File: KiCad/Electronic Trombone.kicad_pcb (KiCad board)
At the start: 2 copper layers, 148 parts, among them J1 691137710004, J2 691137710003, J3 691137710003, J4 691137710002, Q1 NPN, Q2 PNP, Q3 NPN, Q4 PNP, Q5 NPN, Q6 NPN, SW1 SW_Push, SW2 SW_Push, SW3 SW_Push, U1 CD74HC4051E, U10 TL074, U2 TL074, U3 TL074, U4 40106, U5 TL074, U6 TL074, U7 TL074, U8 TL074, U9 TL074

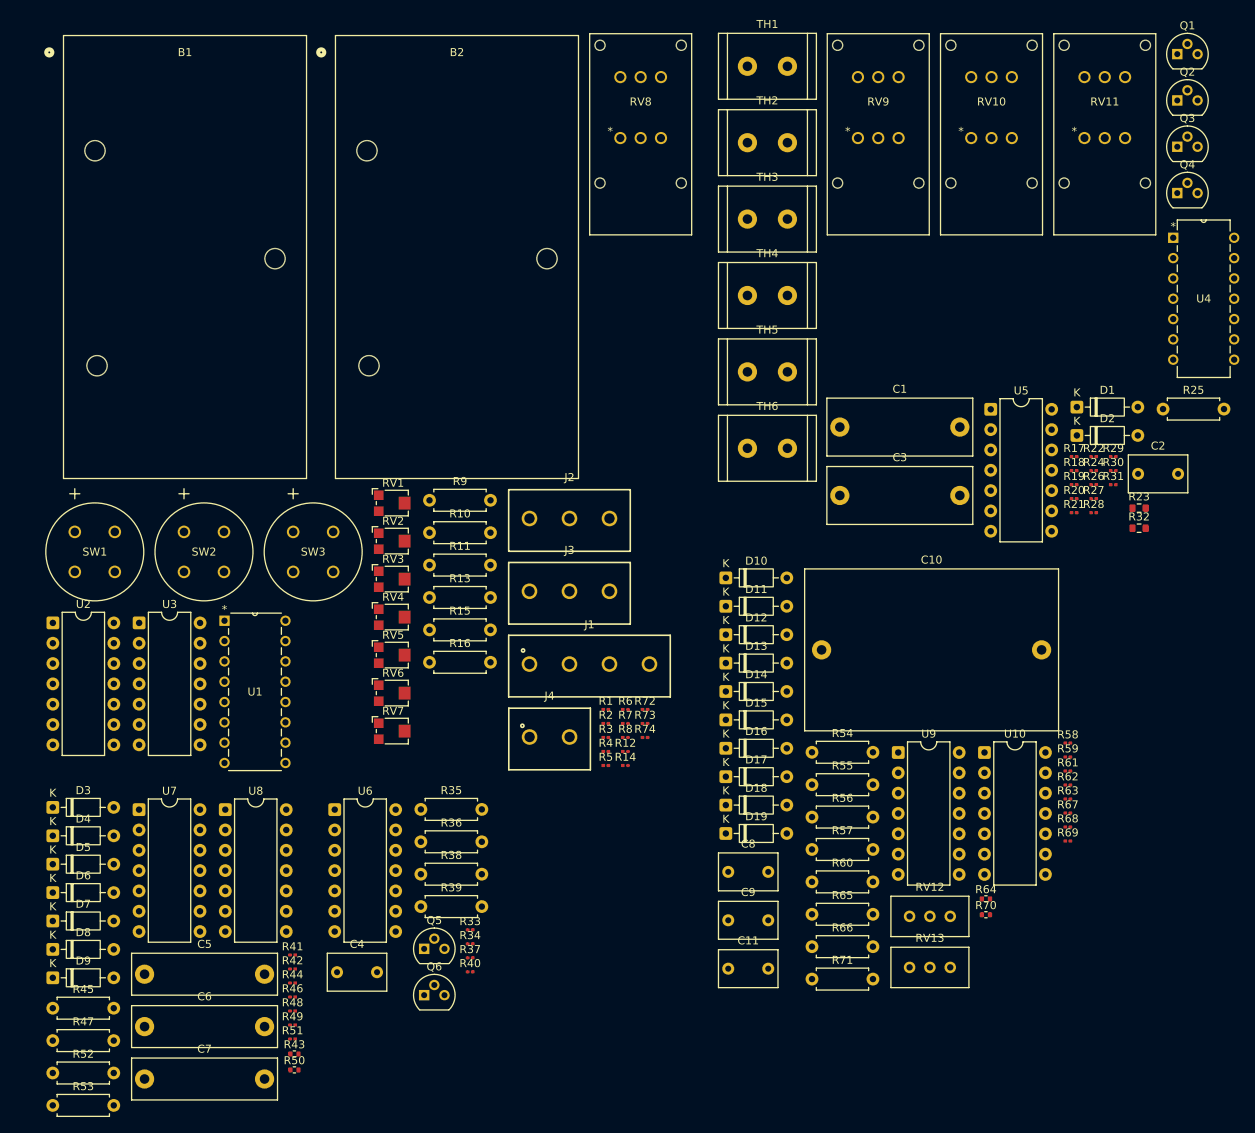
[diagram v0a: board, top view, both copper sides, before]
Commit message: added power switch, decoupling caps, and unused IC pins
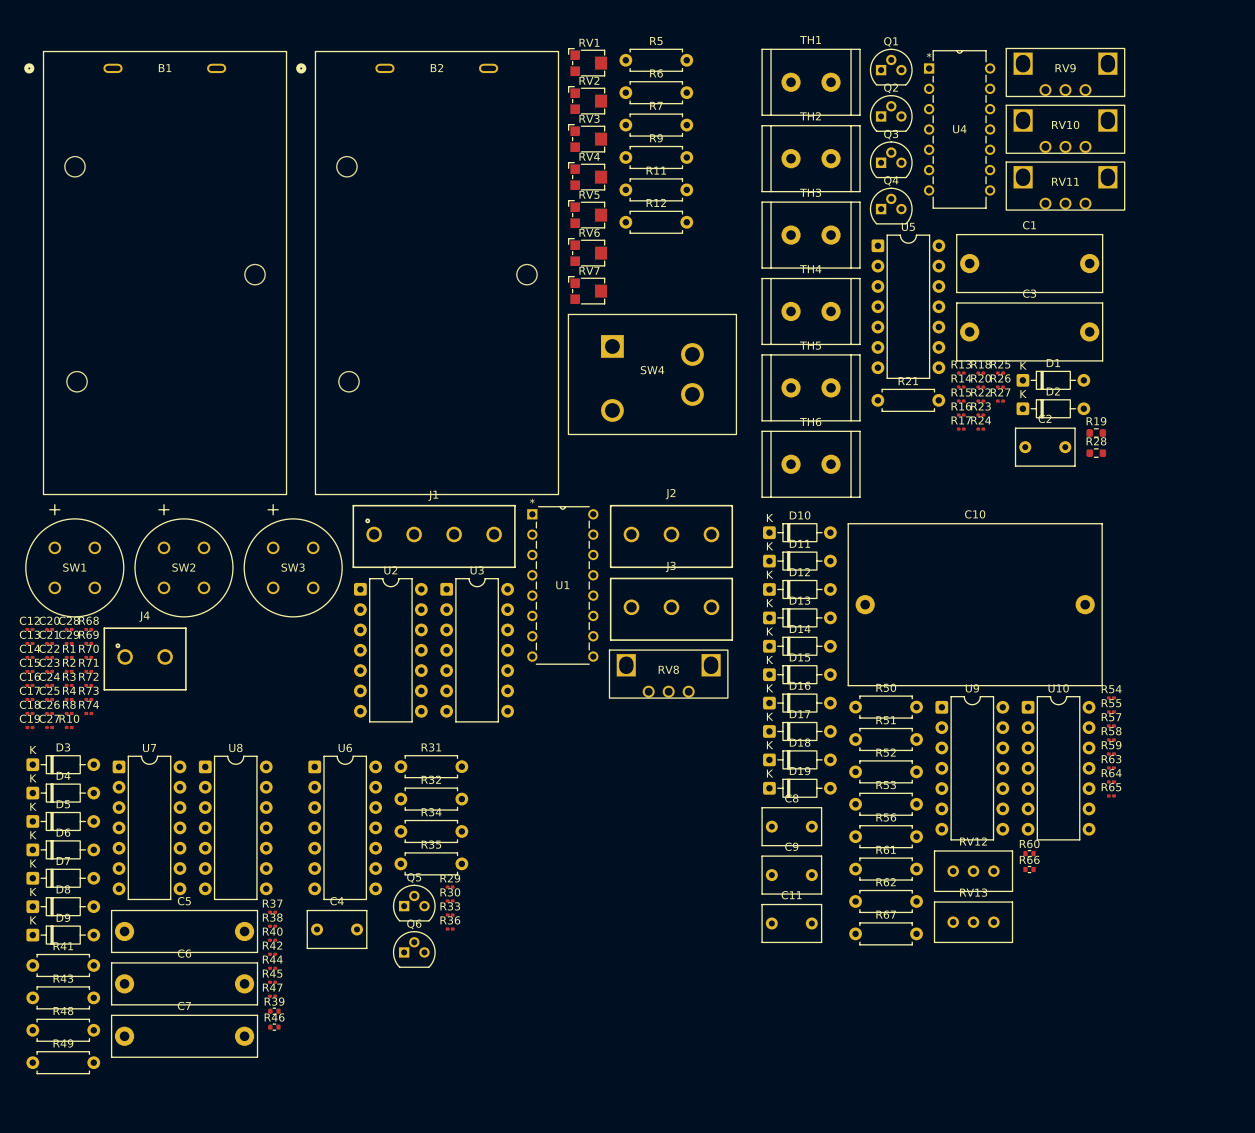
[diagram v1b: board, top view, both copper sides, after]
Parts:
- added C12: 0.1u, Capacitor_SMD:C_0201_0603Metric, F.Cu at (21.2, 98.7)
- added C13: 0.1u, Capacitor_SMD:C_0201_0603Metric, F.Cu at (21.2, 100.4)
- added C14: 0.1u, Capacitor_SMD:C_0201_0603Metric, F.Cu at (21.2, 102.2)
- added C15: 0.1u, Capacitor_SMD:C_0201_0603Metric, F.Cu at (21.2, 103.9)
- added C16: 0.1u, Capacitor_SMD:C_0201_0603Metric, F.Cu at (21.2, 105.7)
- added C17: 0.1u, Capacitor_SMD:C_0201_0603Metric, F.Cu at (21.2, 107.4)
- added C18: 0.1u, Capacitor_SMD:C_0201_0603Metric, F.Cu at (21.2, 109.2)
- added C19: 0.1u, Capacitor_SMD:C_0201_0603Metric, F.Cu at (21.2, 110.9)
- added C20: 0.1u, Capacitor_SMD:C_0201_0603Metric, F.Cu at (23.7, 98.7)
- added C21: 0.1u, Capacitor_SMD:C_0201_0603Metric, F.Cu at (23.7, 100.4)
- added C22: 0.1u, Capacitor_SMD:C_0201_0603Metric, F.Cu at (23.7, 102.2)
- added C23: 0.1u, Capacitor_SMD:C_0201_0603Metric, F.Cu at (23.7, 103.9)
- added C24: 0.1u, Capacitor_SMD:C_0201_0603Metric, F.Cu at (23.7, 105.7)
- added C25: 0.1u, Capacitor_SMD:C_0201_0603Metric, F.Cu at (23.7, 107.4)
- added C26: 0.1u, Capacitor_SMD:C_0201_0603Metric, F.Cu at (23.7, 109.2)
- added C27: 0.1u, Capacitor_SMD:C_0201_0603Metric, F.Cu at (23.7, 110.9)
- added C28: 0.1u, Capacitor_SMD:C_0201_0603Metric, F.Cu at (26.1, 98.7)
- added C29: 0.1u, Capacitor_SMD:C_0201_0603Metric, F.Cu at (26.1, 100.4)
- added SW4: SW_DPST, DPST Switch RA83231100:DPST Switch RA83231100, F.Cu at (99.0, 66.8)
- R1, R4: value 12k -> 10k
- R10, R36: value R_US -> 10k; footprint Resistor_THT:R_Axial_DIN0207_L6.3mm_D2.5mm_P7.62mm_Horizontal -> Resistor_SMD:R_0201_0603Metric
- R12, R5, R6, R7: value 10k -> R_US; footprint Resistor_SMD:R_0201_0603Metric -> Resistor_THT:R_Axial_DIN0207_L6.3mm_D2.5mm_P7.62mm_Horizontal
- R13, R15, R38, R45, R47, R65: value R_US -> 30k; footprint Resistor_THT:R_Axial_DIN0207_L6.3mm_D2.5mm_P7.62mm_Horizontal -> Resistor_SMD:R_0201_0603Metric
- R14: value 10k -> 100k
- R16, R25: value R_US -> 1M; footprint Resistor_THT:R_Axial_DIN0207_L6.3mm_D2.5mm_P7.62mm_Horizontal -> Resistor_SMD:R_0201_0603Metric
- R17, R26: value 30k -> 1M
- R19, R28: value 30k -> 2.5k; footprint Resistor_SMD:R_0201_0603Metric -> Resistor_SMD:R_0603_1608Metric
- R2, R3: value 15k -> 10k
- R20, R29, R30: value 1M -> 100k
- R21: value 1M -> R_US; footprint Resistor_SMD:R_0201_0603Metric -> Resistor_THT:R_Axial_DIN0207_L6.3mm_D2.5mm_P7.62mm_Horizontal
- R22, R24, R37, R58, R59: value 100k -> 30k
- R23: value 2.5k -> 100k; footprint Resistor_SMD:R_0603_1608Metric -> Resistor_SMD:R_0201_0603Metric
- R31, R34: value 100k -> R_US; footprint Resistor_SMD:R_0201_0603Metric -> Resistor_THT:R_Axial_DIN0207_L6.3mm_D2.5mm_P7.62mm_Horizontal
- R32: value 2.5k -> R_US; footprint Resistor_SMD:R_0603_1608Metric -> Resistor_THT:R_Axial_DIN0207_L6.3mm_D2.5mm_P7.62mm_Horizontal
- R39, R60, R66: value R_US -> 1k; footprint Resistor_THT:R_Axial_DIN0207_L6.3mm_D2.5mm_P7.62mm_Horizontal -> Resistor_SMD:R_0402_1005Metric
- R40: value 10k -> 30k
- R41, R48, R49, R51, R62: value 30k -> R_US; footprint Resistor_SMD:R_0201_0603Metric -> Resistor_THT:R_Axial_DIN0207_L6.3mm_D2.5mm_P7.62mm_Horizontal
- R43, R50: value 1k -> R_US; footprint Resistor_SMD:R_0402_1005Metric -> Resistor_THT:R_Axial_DIN0207_L6.3mm_D2.5mm_P7.62mm_Horizontal
- R46: value 30k -> 1k; footprint Resistor_SMD:R_0201_0603Metric -> Resistor_SMD:R_0402_1005Metric
- R54, R55: value R_US -> 100k; footprint Resistor_THT:R_Axial_DIN0207_L6.3mm_D2.5mm_P7.62mm_Horizontal -> Resistor_SMD:R_0201_0603Metric
- R57: value R_US -> 510; footprint Resistor_THT:R_Axial_DIN0207_L6.3mm_D2.5mm_P7.62mm_Horizontal -> Resistor_SMD:R_0201_0603Metric
- R61, R67: value 510 -> R_US; footprint Resistor_SMD:R_0201_0603Metric -> Resistor_THT:R_Axial_DIN0207_L6.3mm_D2.5mm_P7.62mm_Horizontal
- R63: value 30k -> 510
- R64, R70: value 1k -> 30k; footprint Resistor_SMD:R_0402_1005Metric -> Resistor_SMD:R_0201_0603Metric
- R71: value R_US -> 15k; footprint Resistor_THT:R_Axial_DIN0207_L6.3mm_D2.5mm_P7.62mm_Horizontal -> Resistor_SMD:R_0201_0603Metric
- R72, R73: value 30k -> 12k
- R74: value 30k -> 15k
- RV10, RV11, RV8, RV9: footprint Potentiometer 51CAD_E24_A20L:POT_51CAD_12P5X13P25_BRN -> Potentiometer 100k PTV09A-2020F-B104:Potentiometer 100k PTV09A-2020F-B104
- SW1, SW2, SW3: value SW_Push -> SW_Push_Dual
- moved R68 124.8 mm to (28.6, 98.7)
- moved R69 124.8 mm to (28.6, 100.4)
- moved R70 116.7 mm to (28.6, 102.2)
- moved R52 107.2 mm to (124.4, 116.5)
- moved R53 107.2 mm to (124.4, 120.5)
- moved R29 98.8 mm to (73.7, 130.9)
- moved R30 98.8 mm to (73.7, 132.6)
- moved R32 98.3 mm to (67.6, 119.9)
- moved R71 98.2 mm to (28.6, 103.9)
- moved R31 95.8 mm to (67.6, 115.8)
- moved R5 88.2 mm to (95.7, 27.5)
- moved R50 83.5 mm to (124.4, 108.4)
- moved R51 79.7 mm to (124.4, 112.4)
- moved R6 77.1 mm to (95.7, 31.6)
- moved R7 74.8 mm to (95.7, 35.6)
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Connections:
- net Net-(D1-A) renamed //Oscillator/Sch Inv Out 1
- D2 pad 2: Net-(D2-A) -> //Oscillator/Sch Inv Out 2
- R1 pad 1: +5V -> //-Pot
- R1 pad 2: +9V -> Net-(U2B-+)
- R10 pad 1: GND -> Net-(R10-Pad1)
- R10 pad 2: Net-(U2C--) -> Net-(U3C-+)
- R11 pad 2: Net-(R11-Pad2) -> //Amp Control
- R12 pad 1: Net-(U3D-+) -> //Envelope Generator/Out Amp
- R12 pad 2: //Filter Control -> Net-(U3B-+)
- R13 pad 1: //Envelope Generator/Out Filter -> Net-(R13-Pad1)
- R13 pad 2: Net-(U3B-+) -> GND
- R14 pad 1: Net-(R11-Pad2) -> Net-(R13-Pad1)
- R14 pad 2: Net-(U3D-+) -> Net-(R14-Pad2)
- R15 pad 1: Net-(U3C-+) -> -9V
- R15 pad 2: //Amp Control -> Net-(R13-Pad1)
- R16 pad 1: //Envelope Generator/Out Amp -> +9V
- R16 pad 2: Net-(U3C-+) -> Net-(Q1-B)
- R17 pad 2: GND -> Net-(R17-Pad2)
- R18 pad 1: Net-(R17-Pad1) -> //Oscillator/In
- R19 pad 1: -9V -> //Oscillator/Core In 1
- R19 pad 2: Net-(R17-Pad1) -> GND
- R2 pad 1: -5V -> Net-(U2B-+)
- R2 pad 2: GND -> //+Pot
- R20 pad 1: +9V -> Net-(C2-Pad2)
- R20 pad 2: Net-(Q1-B) -> Net-(U5C-+)
- R21 pad 1: Net-(R21-Pad1) -> GND
- R21 pad 2: Net-(R21-Pad2) -> Net-(U5C-+)
- R22 pad 1: //Oscillator/In -> Net-(R22-Pad1)
- R22 pad 2: Net-(R22-Pad2) -> GND
- R23 pad 1: //Oscillator/Core In 1 -> Net-(R22-Pad1)
- R23 pad 2: GND -> Net-(R23-Pad2)
- R24 pad 1: Net-(C2-Pad2) -> -9V
- R24 pad 2: Net-(U5C-+) -> Net-(R22-Pad1)
- R25 pad 1: GND -> +9V
- R25 pad 2: Net-(U5C-+) -> Net-(Q3-B)
- R26 pad 2: GND -> Net-(R26-Pad2)
- R27 pad 1: Net-(R26-Pad1) -> //Oscillator/In
- R28 pad 1: -9V -> //Oscillator/Core In 2
- R28 pad 2: Net-(R26-Pad1) -> GND
- R29 pad 2: Net-(Q3-B) -> Net-(Q5-C)
- R3 pad 2: +5V -> Net-(U2B--)
- R30 pad 1: Net-(R30-Pad1) -> +9V
- R30 pad 2: Net-(R30-Pad2) -> Net-(Q6-C)
- R31 pad 1: //Oscillator/In -> Net-(U6C--)
- R31 pad 2: Net-(R31-Pad2) -> Net-(C4-Pad1)
- R32 pad 1: //Oscillator/Core In 2 -> Net-(U6A--)
- R32 pad 2: GND -> Net-(U6C--)
- R33 pad 1: +9V -> Net-(U6D-+)
- R33 pad 2: Net-(Q5-C) -> GND
- R34 pad 1: +9V -> Net-(U6B--)
- R34 pad 2: Net-(Q6-C) -> Net-(U6C-+)
- R35 pad 1: Net-(U6C--) -> Net-(U6C-+)
- R35 pad 2: Net-(C4-Pad1) -> GND
- R36 pad 1: Net-(U6A--) -> Net-(Q5-E)
- R36 pad 2: Net-(U6C--) -> //Amp Control
- R37 pad 1: Net-(U6D-+) -> Net-(U7B--)
- R37 pad 2: GND -> Net-(D3-A)
- R38 pad 1: Net-(U6B--) -> //Filter/Signal In
- R38 pad 2: Net-(U6C-+) -> Net-(U7B--)
- R39 pad 1: Net-(U6C-+) -> Net-(D3-A)
- R39 pad 2: GND -> Net-(R39-Pad2)
- R4 pad 1: -9V -> Net-(U2B--)
- R4 pad 2: -5V -> //Pot Voltage Difference
- R40 pad 1: Net-(Q5-E) -> Net-(U7B-+)
- R40 pad 2: //Amp Control -> //Filter/Processed Control
- R41 pad 1: Net-(U7B--) -> Net-(D5-A)
- R41 pad 2: Net-(D3-A) -> //Filter Control
- R42 pad 1: //Filter/Signal In -> GND
- R42 pad 2: Net-(U7B--) -> Net-(U7B-+)
- R43 pad 1: Net-(D3-A) -> GND
- R43 pad 2: Net-(R43-Pad2) -> Net-(D5-A)
- R44 pad 1: Net-(U7B-+) -> Net-(U7C--)
- R44 pad 2: //Filter/Processed Control -> Net-(D9-K)
- R45 pad 1: Net-(D5-A) -> //Filter/Signal In
- R45 pad 2: //Filter Control -> Net-(U7C--)
- R46 pad 1: GND -> Net-(D9-K)
- R46 pad 2: Net-(U7B-+) -> Net-(R46-Pad2)
- R47 pad 1: GND -> //Filter/Processed Control
- R47 pad 2: Net-(D5-A) -> Net-(U7C--)
- R48 pad 1: Net-(U7C--) -> Net-(U8B--)
- R48 pad 2: Net-(D9-K) -> Net-(U8C-+)
- R49 pad 1: //Filter/Signal In -> Net-(U8A--)
- R49 pad 2: Net-(U7C--) -> Net-(U8B--)
- R5 pad 1: //-Pot -> Net-(U2C--)
- R5 pad 2: Net-(U2B-+) -> Net-(R5-Pad2)
- R50 pad 1: Net-(D9-K) -> Net-(D10-K)
- R50 pad 2: Net-(R50-Pad2) -> //Envelope Generator/Sustain Voltage Amp
- R51 pad 1: //Filter/Processed Control -> //Envelope Generator/Sustain Voltage Amp
- R51 pad 2: Net-(U7C--) -> GND
- R52 pad 1: Net-(U8B--) -> Net-(D11-K)
- R52 pad 2: Net-(U8C-+) -> //Envelope Generator/Sustain Voltage Filter
- R53 pad 1: Net-(U8A--) -> //Envelope Generator/Sustain Voltage Filter
- R53 pad 2: Net-(U8B--) -> GND
- R54 pad 1: Net-(D10-K) -> GND
- R54 pad 2: //Envelope Generator/Sustain Voltage Amp -> //Envelope Generator/Trigger Ref
- R55 pad 1: //Envelope Generator/Sustain Voltage Amp -> //Envelope Generator/Trigger Ref
- R55 pad 2: GND -> -9V
- R56 pad 1: Net-(D11-K) -> Net-(D12-K)
- R56 pad 2: //Envelope Generator/Sustain Voltage Filter -> Net-(U10B-+)
- R57 pad 1: //Envelope Generator/Sustain Voltage Filter -> Net-(D13-A)
- R57 pad 2: GND -> Net-(R57-Pad2)
- R58 pad 1: GND -> Net-(D13-K)
- R58 pad 2: //Envelope Generator/Trigger Ref -> GND
- R59 pad 1: //Envelope Generator/Trigger Ref -> Net-(D14-K)
- R59 pad 2: -9V -> //Envelope Generator/Sustain Voltage Filter
- R6 pad 1: Net-(U2B-+) -> GND
- R6 pad 2: //+Pot -> Net-(U2C--)
- R60 pad 1: Net-(D12-K) -> Net-(R60-Pad1)
- R60 pad 2: Net-(U10B-+) -> //Envelope Generator/Out Amp
- R61 pad 1: Net-(D13-A) -> Net-(D15-A)
- R61 pad 2: Net-(R61-Pad2) -> Net-(U10B-+)
- R62 pad 1: Net-(D13-K) -> Net-(D16-K)
- R62 pad 2: GND -> Net-(U10D-+)
- R63 pad 1: Net-(D14-K) -> Net-(D17-A)
- R63 pad 2: //Envelope Generator/Sustain Voltage Filter -> Net-(R63-Pad2)
- R64 pad 1: Net-(R64-Pad1) -> Net-(D17-K)
- R64 pad 2: //Envelope Generator/Out Amp -> GND
- R65 pad 1: Net-(D15-A) -> Net-(D18-K)
- R65 pad 2: Net-(U10B-+) -> //Envelope Generator/Sustain Voltage Amp
- R66 pad 1: Net-(D16-K) -> Net-(R66-Pad1)
- R66 pad 2: Net-(U10D-+) -> //Envelope Generator/Out Filter
- R67 pad 1: Net-(D17-A) -> Net-(D19-A)
- R67 pad 2: Net-(R67-Pad2) -> Net-(U10D-+)
- R68 pad 1: Net-(D17-K) -> Net-(J3-Pad1)
- R69 pad 1: Net-(D18-K) -> Net-(J3-Pad2)
- R69 pad 2: //Envelope Generator/Sustain Voltage Amp -> GND
- R7 pad 1: GND -> Net-(U3A-+)
- R7 pad 2: Net-(U2B--) -> Net-(R10-Pad1)
- R70 pad 1: Net-(R70-Pad1) -> Net-(J3-Pad3)
- R70 pad 2: //Envelope Generator/Out Filter -> GND
- R71 pad 1: Net-(D19-A) -> -5V
- R71 pad 2: Net-(U10D-+) -> GND
- R72 pad 1: Net-(J3-Pad1) -> +5V
- R72 pad 2: GND -> +9V
- R73 pad 1: Net-(J3-Pad2) -> -9V
- R73 pad 2: GND -> -5V
- R74 pad 1: Net-(J3-Pad3) -> GND
- R74 pad 2: GND -> +5V
- R8 pad 1: Net-(U2B--) -> Net-(U3C-+)
- R8 pad 2: //Pot Voltage Difference -> //Filter Control
- R9 pad 1: Net-(U2C--) -> //Envelope Generator/Out Filter
- R9 pad 2: Net-(R9-Pad2) -> Net-(U3A-+)
- RV11 pad 2: Net-(R30-Pad1) -> Net-(R26-Pad1)
- RV12 pad 1: Net-(R61-Pad2) -> Net-(R57-Pad2)
- RV12 pad 2: Net-(R61-Pad2) -> Net-(R57-Pad2)
- RV13 pad 1: Net-(R67-Pad2) -> Net-(R63-Pad2)
- RV13 pad 2: Net-(R67-Pad2) -> Net-(R63-Pad2)
- RV8 pad 1: Net-(R9-Pad2) -> Net-(R5-Pad2)
- RV9 pad 2: Net-(R21-Pad1) -> Net-(R17-Pad1)
- SW1 pad 3: (no net) -> +5V
- SW1 pad 4: (no net) -> Net-(J3-Pad1)
- SW2 pad 3: (no net) -> +5V
- SW2 pad 4: (no net) -> Net-(J3-Pad2)
- SW3 pad 3: (no net) -> +5V
- SW3 pad 4: (no net) -> Net-(J3-Pad3)
- TH1 pad 1: Net-(R18-Pad2) -> Net-(R14-Pad2)
- TH2 pad 1: Net-(R21-Pad2) -> Net-(R17-Pad2)
- TH3 pad 1: Net-(R22-Pad2) -> Net-(R18-Pad2)
- TH4 pad 1: Net-(R27-Pad2) -> Net-(R23-Pad2)
- TH5 pad 1: Net-(R30-Pad2) -> Net-(R26-Pad2)
- TH6 pad 1: Net-(R31-Pad2) -> Net-(R27-Pad2)
- U10 pad 11: (no net) -> -9V
- U10 pad 14: Net-(R70-Pad1) -> Net-(R66-Pad1)
- U10 pad 4: (no net) -> +9V
- U10 pad 7: Net-(R64-Pad1) -> Net-(R60-Pad1)
- U2 pad 11: (no net) -> -9V
- U2 pad 4: (no net) -> +9V
- U2 pad 8: Net-(R9-Pad2) -> Net-(R5-Pad2)
- U3 pad 1: (no net) -> Net-(R10-Pad1)
- U3 pad 11: (no net) -> -9V
- U3 pad 12: Net-(U3D-+) -> GND
- U3 pad 13: GND -> Net-(U3D--)
- U3 pad 14: //Filter Control -> Net-(U3D--)
- U3 pad 2: (no net) -> GND
- U3 pad 3: (no net) -> Net-(U3A-+)
- U3 pad 4: (no net) -> +9V
- U3 pad 7: Net-(R11-Pad2) -> //Amp Control
- U3 pad 8: //Amp Control -> //Filter Control
- U4 pad 10: (no net) -> unconnected-(U4-Pad10)
- U4 pad 11: (no net) -> GND
- U4 pad 12: (no net) -> unconnected-(U4-Pad12)
- U4 pad 13: (no net) -> GND
- U4 pad 14: (no net) -> +9V
- U4 pad 3: Net-(D2-K) -> GND
- U4 pad 4: Net-(D2-A) -> unconnected-(U4-Pad4)
- U4 pad 5: (no net) -> GND
- U4 pad 6: (no net) -> unconnected-(U4-Pad6)
- U4 pad 7: (no net) -> -9V
- U4 pad 8: (no net) -> //Oscillator/Sch Inv Out 2
- U4 pad 9: (no net) -> Net-(D2-K)
- U5 pad 11: (no net) -> -9V
- U5 pad 12: (no net) -> GND
- U5 pad 13: (no net) -> Net-(U5D--)
- U5 pad 14: (no net) -> Net-(U5D--)
- U5 pad 4: (no net) -> +9V
- U6 pad 11: (no net) -> -9V
- U6 pad 4: (no net) -> +9V
- U7 pad 11: (no net) -> -9V
- U7 pad 12: (no net) -> GND
- U7 pad 13: (no net) -> Net-(U7D--)
- U7 pad 14: (no net) -> Net-(U7D--)
- U7 pad 4: (no net) -> +9V
- U7 pad 7: Net-(R43-Pad2) -> Net-(R39-Pad2)
- U7 pad 8: Net-(R50-Pad2) -> Net-(R46-Pad2)
- U8 pad 11: (no net) -> -9V
- U8 pad 12: (no net) -> GND
- U8 pad 13: (no net) -> Net-(U8D--)
- U8 pad 14: (no net) -> Net-(U8D--)
- U8 pad 4: (no net) -> +9V
- U9 pad 11: (no net) -> -9V
- U9 pad 4: (no net) -> +9V
